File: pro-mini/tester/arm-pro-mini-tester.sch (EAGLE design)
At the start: 38 parts, among them U1 ARM-PRO-MINI

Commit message: Increased pogo pin holes, added RST and ISP buttons.
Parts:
- added S1, S2: PUSH_BUTTON, arm-pro-mini:PUSH_BUTTON
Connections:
- removed net N$18: D29.C, U1.P0_1
- removed net N$21: D25.C, U1.P0_0
- new net ISP: D29.C, S2.2, U1.P0_1
- new net RST: D25.C, S1.2, U1.P0_0
- net GND: now also S1.1, S2.1
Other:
- note added: "2"
- note removed: "1"
- moved on the sheet: TP1
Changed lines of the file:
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@@
 <part name="R4" library="arm-pro-mini-tester" deviceset="R-US_" device="R0805"/>
 <part name="D17" library="arm-pro-mini-tester" deviceset="LED" device=""/>
+<part name="S2" library="arm-pro-mini" deviceset="PUSH_BUTTON" device=""/>
+<part name="S1" library="arm-pro-mini" deviceset="PUSH_BUTTON" device=""/>
 </parts>
 <sheets>
@@
 <wire x1="340.36" y1="0" x2="0" y2="0" width="0.1524" layer="94"/>
 <wire x1="0" y1="0" x2="0" y2="259.08" width="0.1524" layer="94"/>
-<text x="331.978" y="7.112" size="2.54" layer="97">1</text>
+<text x="331.978" y="7.112" size="2.54" layer="97">2</text>
 <text x="10.16" y="7.62" size="2.54" layer="97" font="vector">OSH. Share alike and attributions are optional. Commercial use ok.</text>
 </plain>
@@
 <instance part="R2" gate="G$1" x="251.46" y="129.54" rot="R270"/>
 <instance part="R3" gate="G$1" x="185.42" y="160.02" rot="R90"/>
-<instance part="TP1" gate="G$1" x="233.68" y="106.68" smashed="yes" rot="R180">
-<attribute name="NAME" x="232.664" y="103.505" size="1.778" layer="95" rot="R180"/>
+<instance part="TP1" gate="G$1" x="208.28" y="106.68" smashed="yes" rot="R180">
+<attribute name="NAME" x="207.264" y="103.505" size="1.778" layer="95" rot="R180"/>
 </instance>
 <instance part="TP2" gate="G$1" x="251.46" y="149.86" smashed="yes" rot="R90">
@@
 <instance part="R4" gate="G$1" x="281.94" y="129.54" rot="R270"/>
 <instance part="D17" gate="G$1" x="281.94" y="119.38" rot="MR0"/>
+<instance part="S2" gate="G$1" x="238.76" y="121.92"/>
+<instance part="S1" gate="G$1" x="226.06" y="121.92"/>
 </instances>
 <busses>
@@
 </segment>
 </net>
-<net name="N$18" class="0">
+<net name="ISP" class="0">
 <segment>
 <pinref part="U1" gate="G$1" pin="P0_1"/>
@@
 <pinref part="D29" gate="G$1" pin="C"/>
 <wire x1="149.86" y1="78.74" x2="170.18" y2="78.74" width="0.1524" layer="91"/>
+<label x="142.24" y="109.22" size="1.778" layer="95"/>
+</segment>
+<segment>
+<pinref part="S2" gate="G$1" pin="2"/>
+<wire x1="238.76" y1="127" x2="238.76" y2="142.24" width="0.1524" layer="91"/>
+<label x="238.76" y="132.08" size="1.778" layer="95" rot="R90"/>
 </segment>
 </net>
@@
 </segment>
 </net>
-<net name="N$21" class="0">
+<net name="RST" class="0">
 <segment>
 <pinref part="U1" gate="G$1" pin="P0_0"/>
@@
 <pinref part="D25" gate="G$1" pin="C"/>
 <wire x1="157.48" y1="101.6" x2="170.18" y2="101.6" width="0.1524" layer="91"/>
+<label x="144.78" y="116.84" size="1.778" layer="95"/>
+</segment>
+<segment>
+<pinref part="S1" gate="G$1" pin="2"/>
+<wire x1="226.06" y1="127" x2="226.06" y2="142.24" width="0.1524" layer="91"/>
+<label x="226.06" y="132.08" size="1.778" layer="95" rot="R90"/>
 </segment>
 </net>
@@
 <wire x1="266.7" y1="106.68" x2="251.46" y2="106.68" width="0.1524" layer="91"/>
 <pinref part="TP1" gate="G$1" pin="TP"/>
-<label x="236.22" y="106.68" size="1.778" layer="95"/>
+<label x="210.82" y="106.68" size="1.778" layer="95"/>
 <pinref part="D17" gate="G$1" pin="C"/>
-<wire x1="251.46" y1="106.68" x2="236.22" y2="106.68" width="0.1524" layer="91"/>
+<wire x1="251.46" y1="106.68" x2="238.76" y2="106.68" width="0.1524" layer="91"/>
+<wire x1="238.76" y1="106.68" x2="226.06" y2="106.68" width="0.1524" layer="91"/>
+<wire x1="226.06" y1="106.68" x2="210.82" y2="106.68" width="0.1524" layer="91"/>
 <wire x1="281.94" y1="114.3" x2="281.94" y2="106.68" width="0.1524" layer="91"/>
 <wire x1="281.94" y1="106.68" x2="266.7" y2="106.68" width="0.1524" layer="91"/>
@@
 <junction x="251.46" y="106.68"/>
 <junction x="266.7" y="106.68"/>
-</segment>
-<segment>
+<pinref part="S1" gate="G$1" pin="1"/>
+<wire x1="226.06" y1="116.84" x2="226.06" y2="106.68" width="0.1524" layer="91"/>
+<pinref part="S2" gate="G$1" pin="1"/>
+<wire x1="238.76" y1="116.84" x2="238.76" y2="106.68" width="0.1524" layer="91"/>
+<junction x="226.06" y="106.68"/>
+<junction x="238.76" y="106.68"/>
+</segment>
+<segment>

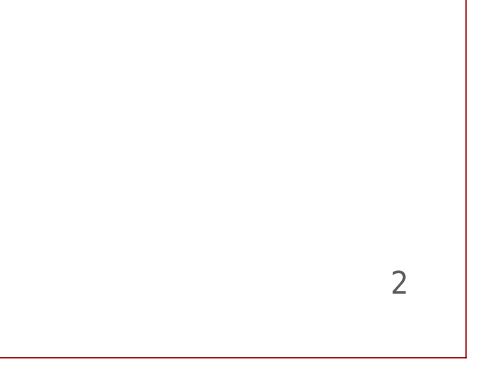
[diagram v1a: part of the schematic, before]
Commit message: Reduced pogo hole sizes from 1.35 mm to ~1mm (40 mil).
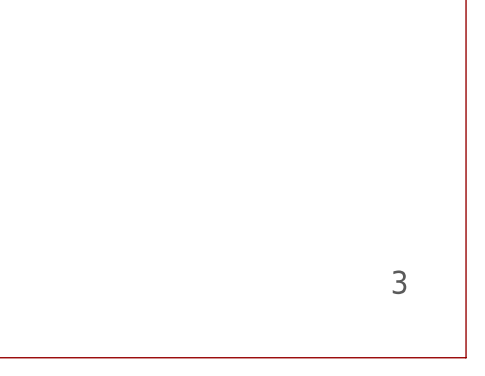
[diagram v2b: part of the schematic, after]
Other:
- note added: "3"
- note removed: "2"
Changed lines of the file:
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@@
 <wire x1="340.36" y1="0" x2="0" y2="0" width="0.1524" layer="94"/>
 <wire x1="0" y1="0" x2="0" y2="259.08" width="0.1524" layer="94"/>
-<text x="331.978" y="7.112" size="2.54" layer="97">2</text>
+<text x="331.978" y="7.112" size="2.54" layer="97">3</text>
 <text x="10.16" y="7.62" size="2.54" layer="97" font="vector">OSH. Share alike and attributions are optional. Commercial use ok.</text>
 </plain>

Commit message: Fixed the tester board. Updated self test for a slow LED scanning.
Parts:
- removed D27, D28, D29, D30: (no value), arm-pro-mini-tester:LED
- removed R4: (no value), arm-pro-mini-tester:R-US_R0805
- removed S1, S2: PUSH_BUTTON, arm-pro-mini:PUSH_BUTTON
- removed TP4: TEST-POINT, arm-pro-mini-tester:TEST-POINT
- added D18: (no value), arm-pro-mini-tester:LED
- R1, R2, R3: value (none) -> 1k5; device arm-pro-mini-tester:R-US_R0805 -> resistor:R-US_R0603
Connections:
- removed net EXT: R4.1, TP4.TP, U1.5V
- removed net ISP: D29.C, S2.2, U1.P0_1
- removed net N$28: D17.A, R4.2
- removed net RST: D25.C, S1.2, U1.P0_0
- net +3.3V: now also R1.2, U1.3.3V; no longer R3.2, U1.GND
- net +5V: now also R3.1, U1.5V; no longer R1.1, U1.EXT
- net GND: now also D25.C, D26.C, U1.GND; no longer D16.C, D17.C, D19.C, S1.1, S2.1, U1.3.3V
- net N$10: now also D11.C; no longer D10.C
- net N$11: now also D10.C; no longer D11.C
- net N$12: now also D6.C; no longer D8.C
- net N$13: now also D7.C; no longer D9.C
- net N$14: now also D9.C; no longer D3.C
- net N$15: now also D8.C; no longer D2.C
- net N$16: now also D19.C; no longer D23.C
- net N$17: now also D24.C; no longer D30.C
- net N$19: now also D23.C; no longer D28.C
- net N$2: now also D2.C; no longer D5.C
- net N$20: now also D22.C; no longer D27.C
- net N$22: now also D21.C; no longer D26.C
- net N$23: now also D20.C; no longer D24.C
- net N$24: now also D18.C; no longer D22.C
- net N$25: now also D17.C; no longer D21.C
- net N$26: now also D16.C; no longer D20.C
- net N$27: now also D16.A, D17.A, D18.A, D19.A, R1.1; no longer D25.A, D26.A, D27.A, D28.A, D29.A, D30.A, R3.1
- net N$29: now also D25.A; no longer D19.A
- net N$3: now also D3.C; no longer D4.C
- net N$31: now also D26.A, R3.2; no longer D16.A, R1.2
- net N$4: now also D4.C; no longer D6.C
- net N$5: now also D5.C; no longer D7.C
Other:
- note added: "3.1"
- note added: "Note: no LEDs for RST and ISP pins."
- note removed: "3"
- moved on the sheet: D10, D11, D16, D17, D19, D2, D20, D21, D22, D23, D24, D25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
